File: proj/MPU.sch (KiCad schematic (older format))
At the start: 30 parts, among them J6 JLINK, U12 ATSAM4S16CA-AU, X2 12MHz

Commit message: Swap 0402 to 0603, add USB inrush protection
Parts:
- removed C126, C127: 15p, IPC7351-Nominal:CAPC1005X55, symbol C-0402
- removed R100, R101, R102, R99: 3k3, IPC7351-Nominal:RESC1005X40, symbol R-0402
- added C66, C67: 15p, IPC7351-Nominal:CAPC1608X55, symbol C-0603
- added R69, R83, R84, R86: 3k3, IPC7351-Nominal:RESC1608X50, symbol R-0603

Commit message: Touch up PCB
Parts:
- removed TP18: GND, conn-test:TEST-SMD-SMALL, symbol TESTPOINT
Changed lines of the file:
@@
 Sheet 13 13
 Title "MPU"
-Date "2015-02-28"
+Date "2015-03-10"
 Rev ""
 Comp "WCP52"
@@
 $EndComp
 $Comp
-L GND #PWR0215
+L GND #PWR0218
 U 1 1 54F6FB24
 P 7500 6900
-F 0 "#PWR0215" H 7500 6900 30  0001 C CNN
+F 0 "#PWR0218" H 7500 6900 30  0001 C CNN
 F 1 "GND" H 7500 6830 30  0001 C CNN
 F 2 "" H 7500 6900 60  0000 C CNN
@@
 $EndComp
 $Comp
-L GND #PWR0216
+L GND #PWR0219
 U 1 1 54F7163B
 P 5200 1950
-F 0 "#PWR0216" H 5200 1950 30  0001 C CNN
+F 0 "#PWR0219" H 5200 1950 30  0001 C CNN
 F 1 "GND" H 5200 1880 30  0001 C CNN
 F 2 "" H 5200 1950 60  0000 C CNN
@@
 $EndComp
 $Comp
-L GND #PWR0217
+L GND #PWR0220
 U 1 1 54F718F9
 P 3450 1950
-F 0 "#PWR0217" H 3450 1950 30  0001 C CNN
+F 0 "#PWR0220" H 3450 1950 30  0001 C CNN
 F 1 "GND" H 3450 1880 30  0001 C CNN
 F 2 "" H 3450 1950 60  0000 C CNN
@@
 $EndComp
 $Comp
-L GND #PWR0218
+L GND #PWR0221
 U 1 1 54F71917
 P 3850 1950
-F 0 "#PWR0218" H 3850 1950 30  0001 C CNN
+F 0 "#PWR0221" H 3850 1950 30  0001 C CNN
 F 1 "GND" H 3850 1880 30  0001 C CNN
 F 2 "" H 3850 1950 60  0000 C CNN
@@
 $EndComp
 $Comp
-L GND #PWR0219
+L GND #PWR0222
 U 1 1 54F7192E
 P 4300 1950
-F 0 "#PWR0219" H 4300 1950 30  0001 C CNN
+F 0 "#PWR0222" H 4300 1950 30  0001 C CNN
 F 1 "GND" H 4300 1880 30  0001 C CNN
 F 2 "" H 4300 1950 60  0000 C CNN
@@
 $EndComp
 $Comp
-L GND #PWR0220
+L GND #PWR0223
 U 1 1 54F71945
 P 4700 1950
-F 0 "#PWR0220" H 4700 1950 30  0001 C CNN
+F 0 "#PWR0223" H 4700 1950 30  0001 C CNN
 F 1 "GND" H 4700 1880 30  0001 C CNN
 F 2 "" H 4700 1950 60  0000 C CNN
@@
 $EndComp
 $Comp
-L GND #PWR0221
+L GND #PWR0224
 U 1 1 54F71A9E
 P 4700 1450
-F 0 "#PWR0221" H 4700 1450 30  0001 C CNN
+F 0 "#PWR0224" H 4700 1450 30  0001 C CNN
 F 1 "GND" H 4700 1380 30  0001 C CNN
 F 2 "" H 4700 1450 60  0000 C CNN
@@
 $EndComp
 $Comp
-L GND #PWR0222
+L GND #PWR0225
 U 1 1 54F72168
 P 3050 1950
-F 0 "#PWR0222" H 3050 1950 30  0001 C CNN
+F 0 "#PWR0225" H 3050 1950 30  0001 C CNN
 F 1 "GND" H 3050 1880 30  0001 C CNN
 F 2 "" H 3050 1950 60  0000 C CNN
@@
 $EndComp
 $Comp
-L GND #PWR0223
+L GND #PWR0226
 U 1 1 54F722F5
 P 3450 2450
-F 0 "#PWR0223" H 3450 2450 30  0001 C CNN
+F 0 "#PWR0226" H 3450 2450 30  0001 C CNN
 F 1 "GND" H 3450 2380 30  0001 C CNN
 F 2 "" H 3450 2450 60  0000 C CNN
@@
 $EndComp
 $Comp
-L GND #PWR0224
+L GND #PWR0227
 U 1 1 54F722FB
 P 3850 2450
-F 0 "#PWR0224" H 3850 2450 30  0001 C CNN
+F 0 "#PWR0227" H 3850 2450 30  0001 C CNN
 F 1 "GND" H 3850 2380 30  0001 C CNN
 F 2 "" H 3850 2450 60  0000 C CNN
@@
 $EndComp
 $Comp
-L GND #PWR0225
+L GND #PWR0228
 U 1 1 54F72301
 P 4250 2450
-F 0 "#PWR0225" H 4250 2450 30  0001 C CNN
+F 0 "#PWR0228" H 4250 2450 30  0001 C CNN
 F 1 "GND" H 4250 2380 30  0001 C CNN
 F 2 "" H 4250 2450 60  0000 C CNN
@@
 $EndComp
 $Comp
-L GND #PWR0226
+L GND #PWR0229
 U 1 1 54F72312
 P 3050 2450
-F 0 "#PWR0226" H 3050 2450 30  0001 C CNN
+F 0 "#PWR0229" H 3050 2450 30  0001 C CNN
 F 1 "GND" H 3050 2380 30  0001 C CNN
 F 2 "" H 3050 2450 60  0000 C CNN
@@
 $EndComp
 $Comp
-L GND #PWR0227
+L GND #PWR0230
 U 1 1 54F73FD5
 P 4800 3750
-F 0 "#PWR0227" H 4800 3750 30  0001 C CNN
+F 0 "#PWR0230" H 4800 3750 30  0001 C CNN
 F 1 "GND" H 4800 3680 30  0001 C CNN
 F 2 "" H 4800 3750 60  0000 C CNN
@@
 $EndComp
 $Comp
-L GND #PWR0228
+L GND #PWR0231
 U 1 1 54F7652D
 P 9550 5850
-F 0 "#PWR0228" H 9550 5850 30  0001 C CNN
+F 0 "#PWR0231" H 9550 5850 30  0001 C CNN
 F 1 "GND" H 9550 5780 30  0001 C CNN
 F 2 "" H 9550 5850 60  0000 C CNN
@@
 $EndComp
 $Comp
-L GND #PWR0229
+L GND #PWR0232
 U 1 1 54F7D5CC
 P 11900 3500
-F 0 "#PWR0229" H 11900 3500 30  0001 C CNN
+F 0 "#PWR0232" H 11900 3500 30  0001 C CNN
 F 1 "GND" H 11900 3430 30  0001 C CNN
 F 2 "" H 11900 3500 60  0000 C CNN
@@
 #RST
 $Comp
-L +3.3SB #PWR0230
-U 1 1 54F7F580
-P 11000 2400
-F 0 "#PWR0230" H 11000 2450 30  0001 C CNN
-F 1 "+3.3SB" H 11000 2500 50  0000 C CNN
-F 2 "" H 11000 2400 60  0000 C CNN
-F 3 "" H 11000 2400 60  0000 C CNN
-	1    11000 2400
-	1    0    0    -1
-$EndComp
-$Comp
-L +3.3SB #PWR0231
+L +3.3SB #PWR0233
 U 1 1 54F7FA68
 P 4700 1150
-F 0 "#PWR0231" H 4700 1200 30  0001 C CNN
+F 0 "#PWR0233" H 4700 1200 30  0001 C CNN
 F 1 "+3.3SB" H 4700 1250 50  0000 C CNN
 F 2 "" H 4700 1150 60  0000 C CNN
@@
 $EndComp
 $Comp
-L +3.3SB #PWR0232
+L +3.3SB #PWR0234
 U 1 1 54F7FAA1
 P 6100 1450
-F 0 "#PWR0232" H 6100 1500 30  0001 C CNN
+F 0 "#PWR0234" H 6100 1500 30  0001 C CNN
 F 1 "+3.3SB" H 6100 1550 50  0000 C CNN
 F 2 "" H 6100 1450 60  0000 C CNN
@@
 $EndComp
 $Comp
-L +3.3SB #PWR0233
+L +3.3SB #PWR0235
 U 1 1 54F7FEDA
 P 4300 3350
-F 0 "#PWR0233" H 4300 3400 30  0001 C CNN
+F 0 "#PWR0235" H 4300 3400 30  0001 C CNN
 F 1 "+3.3SB" H 4300 3450 50  0000 C CNN
 F 2 "" H 4300 3350 60  0000 C CNN
@@
 $EndComp
 $Comp
-L +3.3SB #PWR0234
+L +3.3SB #PWR0236
 U 1 1 54F806BD
 P 3050 2150
-F 0 "#PWR0234" H 3050 2200 30  0001 C CNN
+F 0 "#PWR0236" H 3050 2200 30  0001 C CNN
 F 1 "+3.3SB" H 3050 2250 50  0000 C CNN
 F 2 "" H 3050 2150 60  0000 C CNN
@@
 $EndComp
 $Comp
-L +3.3SB #PWR0235
+L +3.3SB #PWR0237
 U 1 1 54F806EC
 P 3450 2150
-F 0 "#PWR0235" H 3450 2200 30  0001 C CNN
+F 0 "#PWR0237" H 3450 2200 30  0001 C CNN
 F 1 "+3.3SB" H 3450 2250 50  0000 C CNN
 F 2 "" H 3450 2150 60  0000 C CNN
@@
 $EndComp
 $Comp
-L +3.3SB #PWR0236
+L +3.3SB #PWR0238
 U 1 1 54F8071B
 P 3850 2150
-F 0 "#PWR0236" H 3850 2200 30  0001 C CNN
+F 0 "#PWR0238" H 3850 2200 30  0001 C CNN
 F 1 "+3.3SB" H 3850 2250 50  0000 C CNN
 F 2 "" H 3850 2150 60  0000 C CNN
@@
 $EndComp
 $Comp
-L +3.3SB #PWR0237
+L +3.3SB #PWR0239
 U 1 1 54F8074A
 P 4250 2150
-F 0 "#PWR0237" H 4250 2200 30  0001 C CNN
+F 0 "#PWR0239" H 4250 2200 30  0001 C CNN
 F 1 "+3.3SB" H 4250 2250 50  0000 C CNN
 F 2 "" H 4250 2150 60  0000 C CNN
@@
 $EndComp
 $Comp
-L +3.3SB #PWR0238
+L +3.3SB #PWR0240
 U 1 1 54F82AC0
 P 8500 2250
-F 0 "#PWR0238" H 8500 2300 30  0001 C CNN
+F 0 "#PWR0240" H 8500 2300 30  0001 C CNN
 F 1 "+3.3SB" H 8500 2350 50  0000 C CNN
 F 2 "" H 8500 2250 60  0000 C CNN
@@
 $EndComp
 $Comp
-L +3.3SB #PWR0239
+L +3.3SB #PWR0241
 U 1 1 54F831D3
 P 8900 2250
-F 0 "#PWR0239" H 8900 2300 30  0001 C CNN
+F 0 "#PWR0241" H 8900 2300 30  0001 C CNN
 F 1 "+3.3SB" H 8900 2350 50  0000 C CNN
 F 2 "" H 8900 2250 60  0000 C CNN
@@
 Connection ~ 11900 3400
 Wire Wire Line
-	11000 2500 11400 2500
-Wire Wire Line
 	11000 2600 11400 2600
 Wire Wire Line
@@
 Wire Wire Line
 	9200 3200 11400 3200
-Wire Wire Line
-	11000 2400 11000 2500
 Wire Wire Line
 	8500 2500 8500 5400
@@
 Connection ~ 9000 2700
 $Comp
-L GND #PWR0240
+L GND #PWR0242
 U 1 1 54F83DA7
 P 9000 3450
-F 0 "#PWR0240" H 9000 3450 30  0001 C CNN
+F 0 "#PWR0242" H 9000 3450 30  0001 C CNN
 F 1 "GND" H 9000 3380 30  0001 C CNN
 F 2 "" H 9000 3450 60  0000 C CNN
@@
 	9000 3450 9000 3400
 $Comp
-L GND #PWR0241
+L GND #PWR0243
 U 1 1 54F83E68
 P 11000 3000
-F 0 "#PWR0241" H 11000 3000 30  0001 C CNN
+F 0 "#PWR0243" H 11000 3000 30  0001 C CNN
 F 1 "GND" H 11000 2930 30  0001 C CNN
 F 2 "" H 11000 3000 60  0000 C CNN
@@
 	9200 2500 9200 3200
 $Comp
-L +3.3SB #PWR0242
+L +3.3SB #PWR0244
 U 1 1 54F86D9A
 P 9200 2250
-F 0 "#PWR0242" H 9200 2300 30  0001 C CNN
+F 0 "#PWR0244" H 9200 2300 30  0001 C CNN
 F 1 "+3.3SB" H 9200 2350 50  0000 C CNN
 F 2 "" H 9200 2250 60  0000 C CNN
@@
 Connection ~ 5600 4200
 $Comp
-L TESTPOINT TP18
-U 1 1 54FD1458
-P 4800 5700
-F 0 "TP18" H 4800 6050 50  0000 C CNN
-F 1 "GND" H 4800 5950 50  0000 C CNN
-F 2 "conn-test:TEST-SMD-SMALL" H 4800 5700 50  0001 C CNN
-F 3 "" H 4800 5700 50  0000 C CNN
-	1    4800 5700
-	1    0    0    -1
-$EndComp
-$Comp
-L GND #PWR0243
-U 1 1 54FD14B5
-P 4800 5750
-F 0 "#PWR0243" H 4800 5750 30  0001 C CNN
-F 1 "GND" H 4800 5680 30  0001 C CNN
-F 2 "" H 4800 5750 60  0000 C CNN
-F 3 "" H 4800 5750 60  0000 C CNN
-	1    4800 5750
-	1    0    0    -1
-$EndComp
-Wire Wire Line
-	4800 5750 4800 5700
-$Comp
 L TESTPOINT TP19
 U 1 1 54FD5BDD
@@
 	1    0    0    -1
 $EndComp
+$Comp
+L +3.3SB #PWR0245
+U 1 1 54FEC56D
+P 11100 2450
+F 0 "#PWR0245" H 11100 2500 30  0001 C CNN
+F 1 "+3.3SB" H 11100 2550 50  0000 C CNN
+F 2 "" H 11100 2450 60  0000 C CNN
+F 3 "" H 11100 2450 60  0000 C CNN
+	1    11100 2450
+	1    0    0    -1
+$EndComp
+Wire Wire Line
+	11400 2500 11100 2500
+Wire Wire Line
+	11100 2500 11100 2450
 $EndSCHEMATC

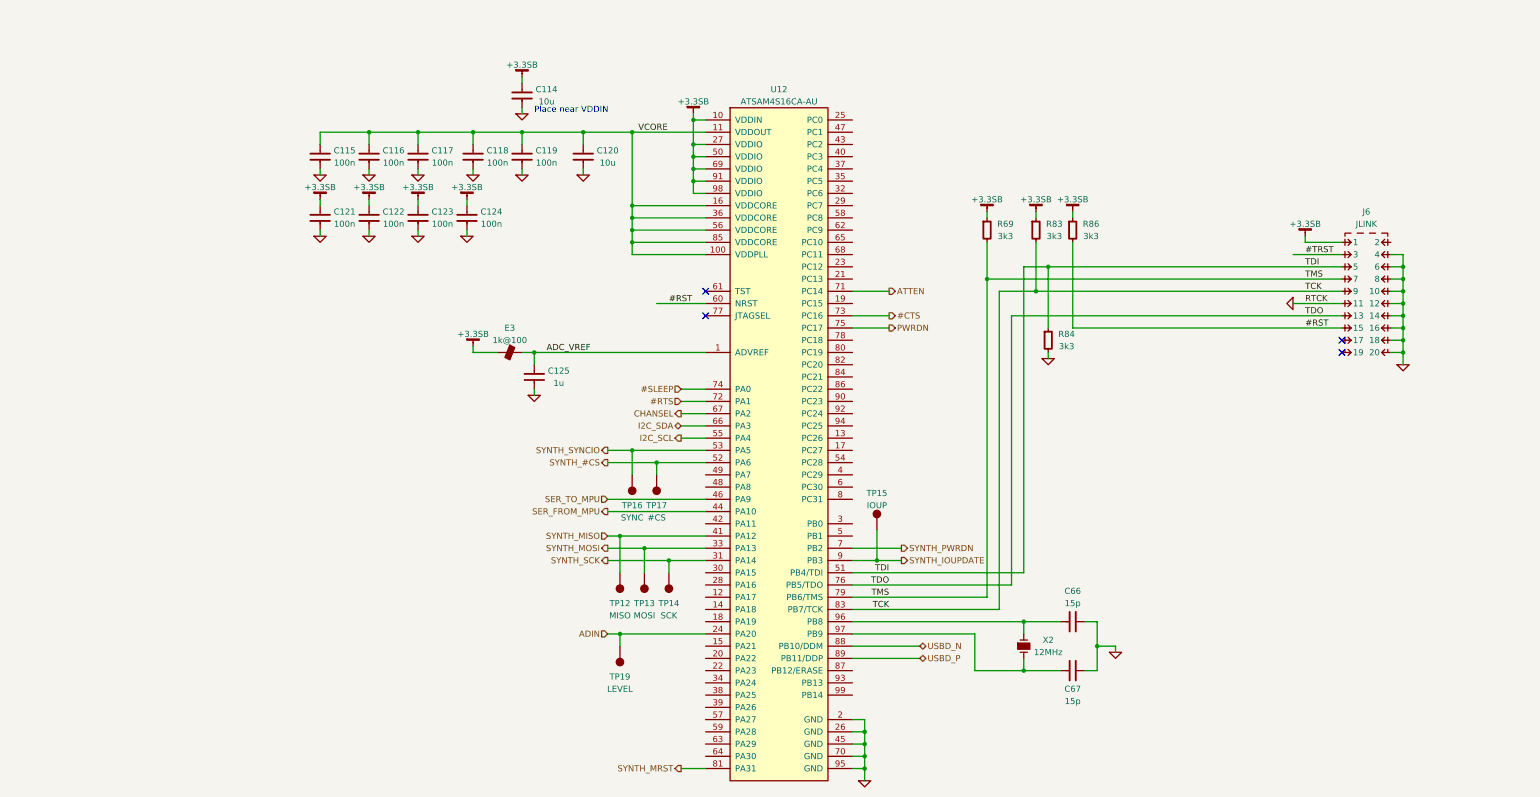
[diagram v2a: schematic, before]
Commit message: Add test LEDs
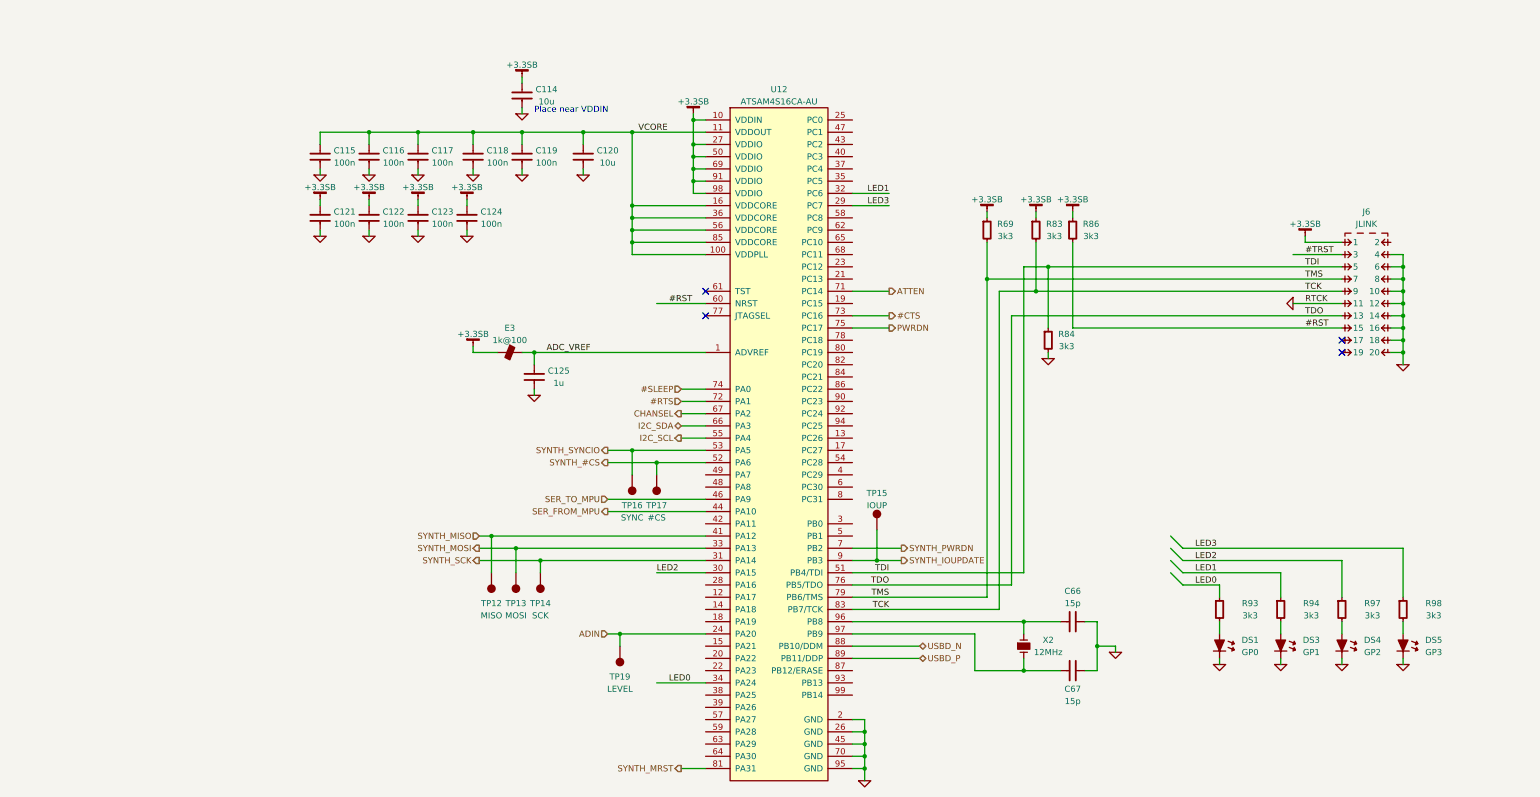
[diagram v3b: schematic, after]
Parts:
- added DS1: GP0, smd-semi:LED-0603, symbol LED-0603
- added DS3: GP1, smd-semi:LED-0603, symbol LED-0603
- added DS4: GP2, smd-semi:LED-0603, symbol LED-0603
- added DS5: GP3, smd-semi:LED-0603, symbol LED-0603
- added R93, R94, R97, R98: 3k3, IPC7351-Nominal:RESC1608X50, symbol R-0603
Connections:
- net GND: now also DS1.1, DS3.1, DS4.1, DS5.1
- net LED3: now reaches U12.29 (PC7)
- net LED3: now also R98.1
- net LED2: now reaches U12.30 (PA15)
- net LED2: now also R97.1
- net LED1: now reaches U12.32 (PC6)
- net LED1: now also R94.1
- net LED0: now reaches U12.34 (PA24)
- net LED0: now also R93.1
- new net: DS1.2, R93.2
- new net: DS3.2, R94.2
- new net: DS4.2, R97.2
- new net: DS5.2, R98.2
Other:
- moved on the sheet: TP12, TP13, TP14
